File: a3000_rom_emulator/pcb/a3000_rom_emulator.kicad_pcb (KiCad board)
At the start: 4 copper layers, 43.2 x 78.7 mm, 86 parts

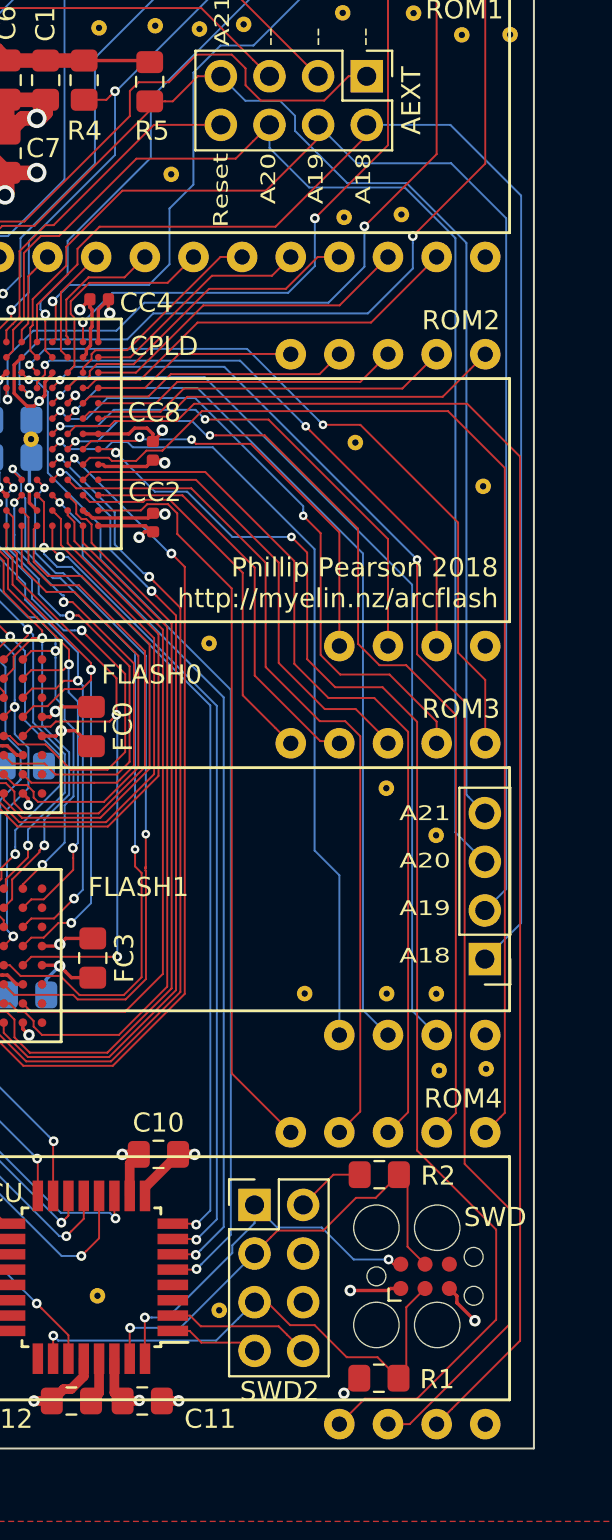
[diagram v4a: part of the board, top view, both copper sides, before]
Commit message: Added some more via staples
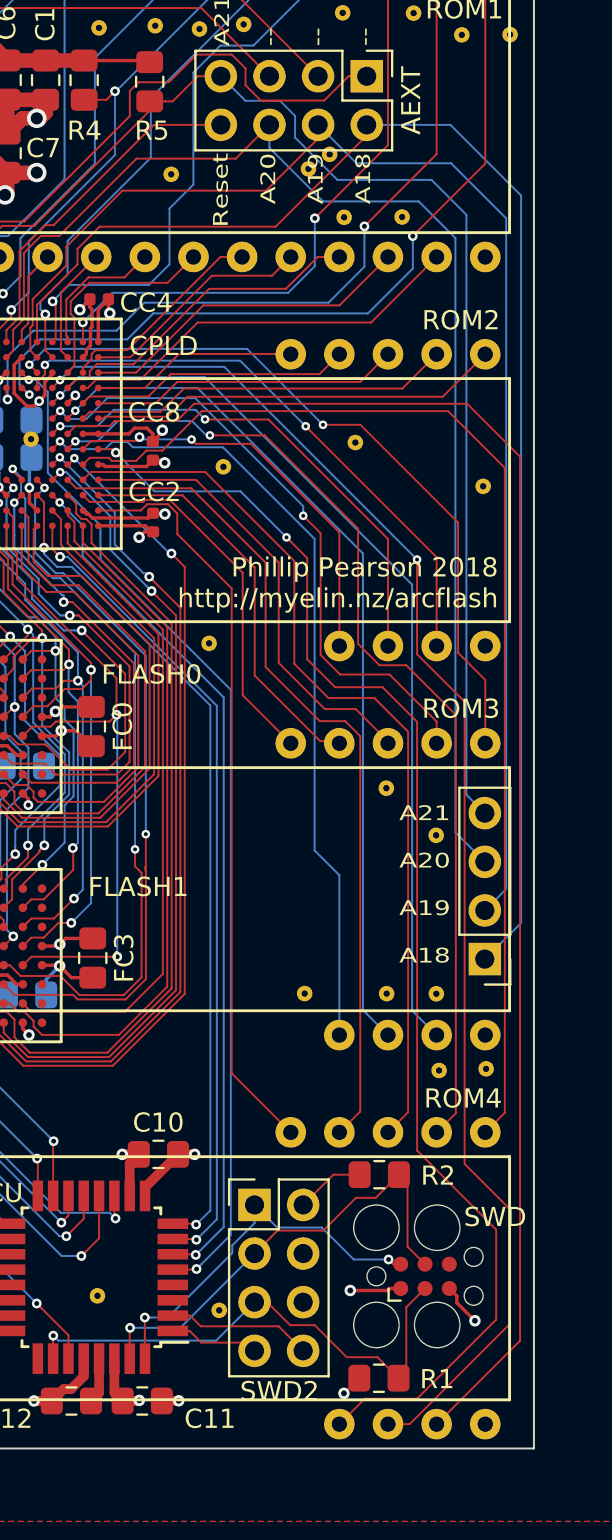
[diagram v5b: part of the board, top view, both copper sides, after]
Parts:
- added staple_single34: , myelin-kicad:via_single, F.Cu at (171.1, 41.1)
- added staple_single35: , myelin-kicad:via_single, F.Cu at (172.2, 40.4)
- added staple_single36: , myelin-kicad:via_single, F.Cu at (166.7, 56.7)
- moved staple_single15 0.14 mm to (176.0, 43.6)
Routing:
- net rom_A19: track 69.1 -> 70.2 mm

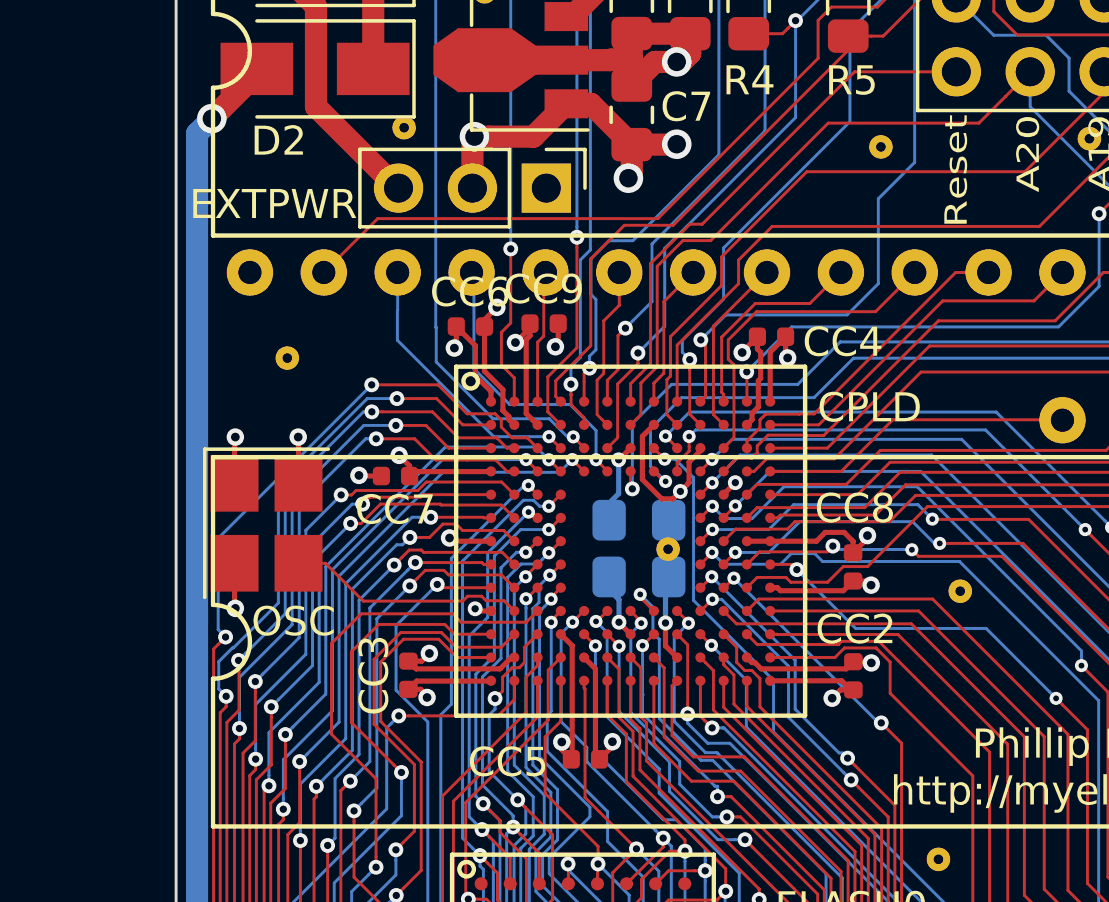
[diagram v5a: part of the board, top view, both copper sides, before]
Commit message: tidied some silkscreen and regenerated renders
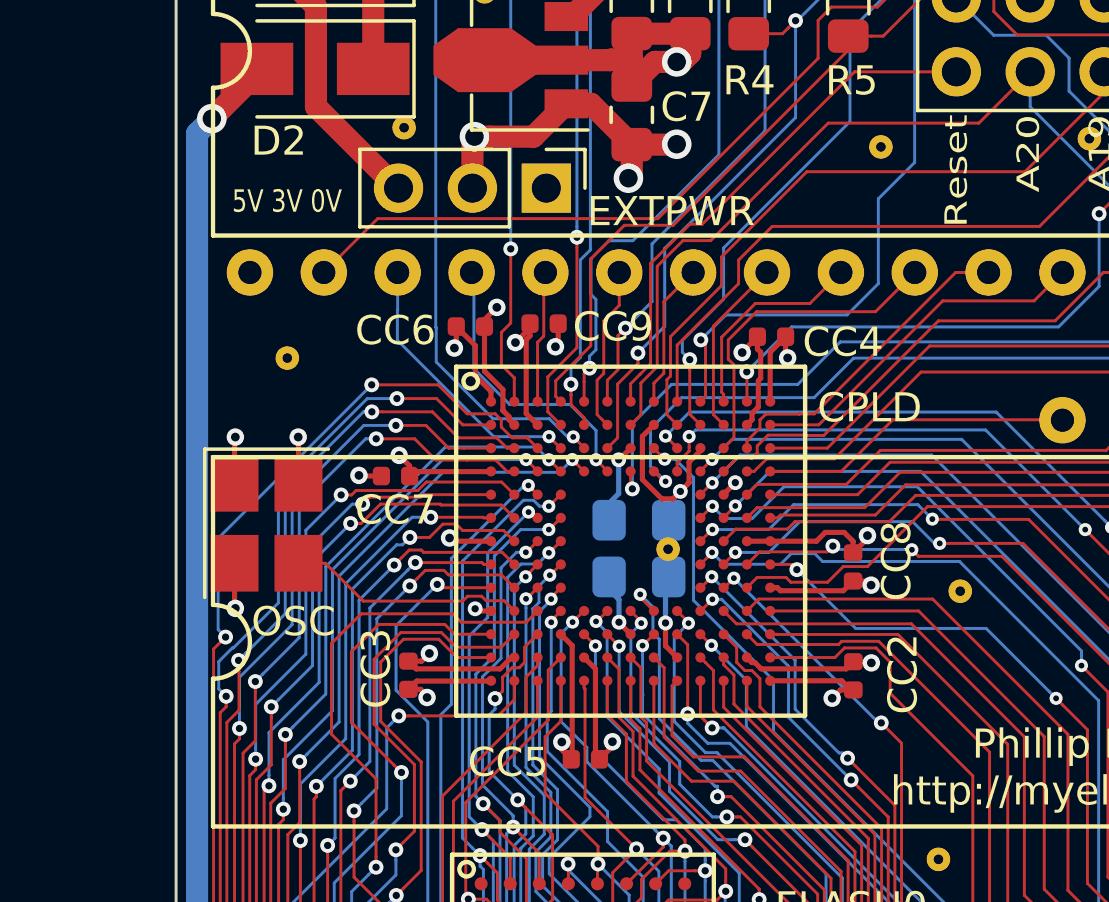
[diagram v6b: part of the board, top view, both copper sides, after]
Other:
- board text added: "5V 3V 0V"
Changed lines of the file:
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@@
   (general
     (thickness 1.6)
-    (drawings 11)
+    (drawings 12)
     (tracks 2467)
     (zones 0)
@@
     (tags capacitor)
     (attr smd)
-    (fp_text reference CC3 (at 0 -1.17 90) (layer F.SilkS)
+    (fp_text reference CC3 (at 0.232 -1.101 270) (layer F.SilkS)
       (effects (font (size 1 1) (thickness 0.15)))
     )
@@
     (descr "Through hole straight pin header, 1x03, 2.54mm pitch, single row")
     (tags "Through hole pin header THT 1x03 2.54mm single row")
-    (fp_text reference EXTPWR (at 0.56574 9.38482) (layer F.SilkS)
+    (fp_text reference EXTPWR (at 0.81 -4.287) (layer F.SilkS)
       (effects (font (size 1 1) (thickness 0.15)))
     )
@@
     (tags capacitor)
     (attr smd)
-    (fp_text reference CC6 (at 0 -1.17) (layer F.SilkS)
+    (fp_text reference CC6 (at -2.573 0.141) (layer F.SilkS)
       (effects (font (size 1 1) (thickness 0.15)))
     )
@@
     (tags capacitor)
     (attr smd)
-    (fp_text reference CC8 (at 2.00716 0.07022 180) (layer F.SilkS)
+    (fp_text reference CC8 (at 0.205 1.499 270) (layer F.SilkS)
       (effects (font (size 1 1) (thickness 0.15)))
     )
@@
     (tags capacitor)
     (attr smd)
-    (fp_text reference CC9 (at 0 -1.17) (layer F.SilkS)
+    (fp_text reference CC9 (at 2.38 0.115) (layer F.SilkS)
       (effects (font (size 1 1) (thickness 0.15)))
     )
@@
     (tags capacitor)
     (attr smd)
-    (fp_text reference CC2 (at 1.58656 0.08562 180) (layer F.SilkS)
+    (fp_text reference CC2 (at 0.064 1.709 270) (layer F.SilkS)
       (effects (font (size 1 1) (thickness 0.15)))
     )
@@
       (net 27 GND) (zone_connect 2))
   )
+  (gr_text "5V 3V 0V" (at 143.514 43.274) (layer F.SilkS)
+    (effects (font (size 0.77 0.6) (thickness 0.1)))
+  )
   (gr_text "A21\n\nA20\n\nA19\n\nA18" (at 178.53152 78.49362) (layer F.SilkS)
